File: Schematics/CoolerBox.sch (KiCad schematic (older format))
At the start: 5 parts, among them J5 12VDC Kfz, J6 12VDC Kfz, SW1 S1

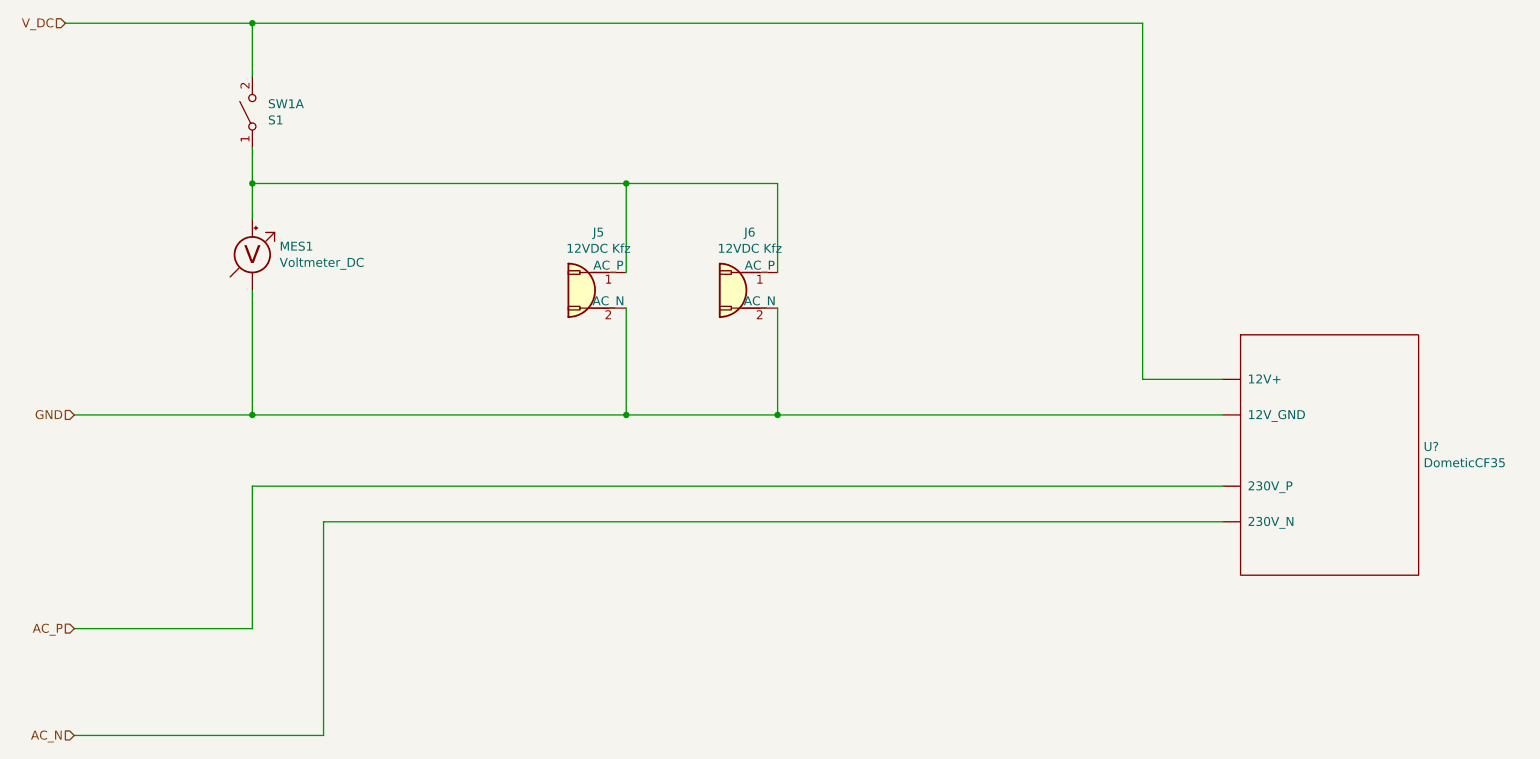
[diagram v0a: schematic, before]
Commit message: add usb charger
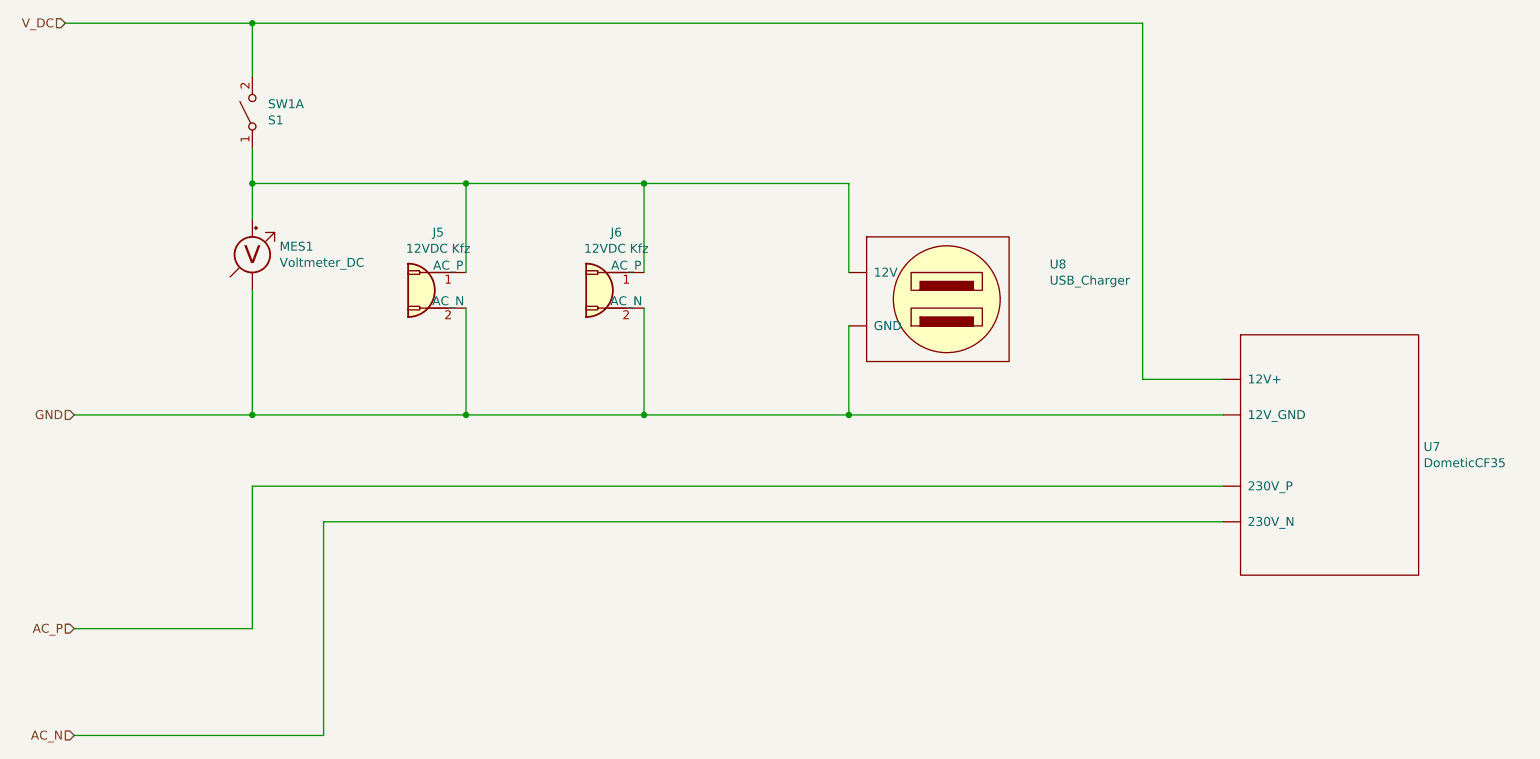
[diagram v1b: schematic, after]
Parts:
- added U8: USB_Charger, symbol MyParts:USB_Charger
- gave numbers to parts that had none: 1
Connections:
- net GND: now also U8.~ (GND)
- net at J5.1 (AC_P), J6.1 (AC_P), MES1.2 (+)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: now also U8.~ (GND)
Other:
- moved on the sheet: J5, J6
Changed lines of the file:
@@
 L Connector:Conn_WallSocket J5
 U 1 1 5EF09B1F
-P 4900 3000
-F 0 "J5" H 4856 3325 50  0000 C CNN
-F 1 "12VDC Kfz" H 4856 3234 50  0000 C CNN
-F 2 "" H 4500 3000 50  0001 C CNN
-F 3 "~" H 4500 3000 50  0001 C CNN
-	1    4900 3000
+P 4000 3000
+F 0 "J5" H 3956 3325 50  0000 C CNN
+F 1 "12VDC Kfz" H 3956 3234 50  0000 C CNN
+F 2 "" H 3600 3000 50  0001 C CNN
+F 3 "~" H 3600 3000 50  0001 C CNN
+	1    4000 3000
 	-1   0    0    -1
 $EndComp
@@
 L Connector:Conn_WallSocket J6
 U 1 1 5EF0A29B
-P 5750 3000
-F 0 "J6" H 5706 3325 50  0000 C CNN
-F 1 "12VDC Kfz" H 5706 3234 50  0000 C CNN
-F 2 "" H 5350 3000 50  0001 C CNN
-F 3 "~" H 5350 3000 50  0001 C CNN
-	1    5750 3000
+P 5000 3000
+F 0 "J6" H 4956 3325 50  0000 C CNN
+F 1 "12VDC Kfz" H 4956 3234 50  0000 C CNN
+F 2 "" H 4600 3000 50  0001 C CNN
+F 3 "~" H 4600 3000 50  0001 C CNN
+	1    5000 3000
 	-1   0    0    -1
 $EndComp
@@
 	3000 3700 3000 3000
 Wire Wire Line
-	3000 2400 5100 2400
+	3000 2400 4200 2400
 Wire Wire Line
-	5100 2400 5100 2900
+	4200 2400 4200 2900
 Connection ~ 3000 2400
 Wire Wire Line
 	3000 2400 3000 2600
 Wire Wire Line
-	5100 2400 5950 2400
+	5200 2400 5200 2900
 Wire Wire Line
-	5950 2400 5950 2900
-Connection ~ 5100 2400
+	3000 3700 4200 3700
 Wire Wire Line
-	3000 3700 5100 3700
-Wire Wire Line
-	5100 3700 5100 3100
+	4200 3700 4200 3100
 Connection ~ 3000 3700
 Wire Wire Line
-	5100 3700 5950 3700
-Wire Wire Line
-	5950 3700 5950 3100
-Connection ~ 5100 3700
+	5200 3700 5200 3100
 Text HLabel 2000 4900 0    50   Input ~ 0
 AC_P
@@
 AC_N
 $Comp
-L MyParts:DometicCF35 U?
+L MyParts:DometicCF35 U7
 U 1 1 5EF0EA96
 P 9000 3350
-F 0 "U?" H 9578 2821 50  0000 L CNN
+F 0 "U7" H 9578 2821 50  0000 L CNN
 F 1 "DometicCF35" H 9578 2730 50  0000 L CNN
 F 2 "" H 9000 3350 50  0001 C CNN
@@
 	3400 4300 8450 4300
 Wire Wire Line
-	3000 1500 8000 1500
-Wire Wire Line
 	8000 1500 8000 3500
 Wire Wire Line
 	8000 3500 8450 3500
 Connection ~ 3000 1500
+$Comp
+L MyParts:USB_Charger U8
+U 1 1 5EF0F9B5
+P 6950 2300
+F 0 "U8" H 7478 1746 50  0000 L CNN
+F 1 "USB_Charger" H 7478 1655 50  0000 L CNN
+F 2 "" H 6950 2300 50  0001 C CNN
+F 3 "" H 6950 2300 50  0001 C CNN
+	1    6950 2300
+	1    0    0    -1
+$EndComp
 Wire Wire Line
-	5950 3700 8450 3700
-Connection ~ 5950 3700
+	6350 2900 6350 2400
+Wire Wire Line
+	6350 3200 6350 3700
+Connection ~ 6350 3700
+Wire Wire Line
+	6350 3700 8450 3700
+Wire Wire Line
+	3000 1500 8000 1500
+Connection ~ 4200 2400
+Connection ~ 4200 3700
+Wire Wire Line
+	4200 2400 5200 2400
+Wire Wire Line
+	4200 3700 5200 3700
+Connection ~ 5200 2400
+Connection ~ 5200 3700
+Wire Wire Line
+	5200 3700 6350 3700
+Wire Wire Line
+	5200 2400 6350 2400
 $EndSCHEMATC

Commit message: add filed
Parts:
- removed U7: DometicCF35, symbol MyParts:DometicCF35
- removed U8: USB_Charger, symbol MyParts:USB_Charger
- renumbered J5 to J?, J6 to J?, MES1 to MES?, SW1 to SW?
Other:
- moved on the sheet: J?
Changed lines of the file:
@@
 $Descr A4 11693 8268
 encoding utf-8
-Sheet 2 3
+Sheet 3 3
 Title ""
 Date ""
@@
 $EndDescr
 $Comp
-L Connector:Conn_WallSocket J5
+L Connector:Conn_WallSocket J?
 U 1 1 5EF09B1F
-P 4000 3000
-F 0 "J5" H 3956 3325 50  0000 C CNN
-F 1 "12VDC Kfz" H 3956 3234 50  0000 C CNN
-F 2 "" H 3600 3000 50  0001 C CNN
-F 3 "~" H 3600 3000 50  0001 C CNN
-	1    4000 3000
+P 4900 3000
+F 0 "J?" H 4856 3325 50  0000 C CNN
+F 1 "12VDC Kfz" H 4856 3234 50  0000 C CNN
+F 2 "" H 4500 3000 50  0001 C CNN
+F 3 "~" H 4500 3000 50  0001 C CNN
+	1    4900 3000
 	-1   0    0    -1
 $EndComp
 $Comp
-L Connector:Conn_WallSocket J6
+L Connector:Conn_WallSocket J?
 U 1 1 5EF0A29B
-P 5000 3000
-F 0 "J6" H 4956 3325 50  0000 C CNN
-F 1 "12VDC Kfz" H 4956 3234 50  0000 C CNN
-F 2 "" H 4600 3000 50  0001 C CNN
-F 3 "~" H 4600 3000 50  0001 C CNN
-	1    5000 3000
+P 5750 3000
+F 0 "J?" H 5706 3325 50  0000 C CNN
+F 1 "12VDC Kfz" H 5706 3234 50  0000 C CNN
+F 2 "" H 5350 3000 50  0001 C CNN
+F 3 "~" H 5350 3000 50  0001 C CNN
+	1    5750 3000
 	-1   0    0    -1
 $EndComp
 $Comp
-L Device:Voltmeter_DC MES1
+L Device:Voltmeter_DC MES?
 U 1 1 5EF0A912
 P 3000 2800
-F 0 "MES1" H 3153 2846 50  0000 L CNN
+F 0 "MES?" H 3153 2846 50  0000 L CNN
 F 1 "Voltmeter_DC" H 3153 2755 50  0000 L CNN
 F 2 "" V 3000 2900 50  0001 C CNN
@@
 $EndComp
 $Comp
-L Switch:SW_DPST_x2 SW1
+L Switch:SW_DPST_x2 SW?
 U 1 1 5EF0B26F
 P 3000 2000
-F 0 "SW1" V 3046 1912 50  0000 R CNN
+F 0 "SW?" V 3046 1912 50  0000 R CNN
 F 1 "S1" V 2955 1912 50  0000 R CNN
 F 2 "" H 3000 2000 50  0001 C CNN
@@
 	3000 3700 3000 3000
 Wire Wire Line
-	3000 2400 4200 2400
+	3000 2400 5100 2400
 Wire Wire Line
-	4200 2400 4200 2900
+	5100 2400 5100 2900
 Connection ~ 3000 2400
 Wire Wire Line
 	3000 2400 3000 2600
 Wire Wire Line
-	5200 2400 5200 2900
+	5100 2400 5950 2400
 Wire Wire Line
-	3000 3700 4200 3700
+	5950 2400 5950 2900
+Connection ~ 5100 2400
 Wire Wire Line
-	4200 3700 4200 3100
+	3000 3700 5100 3700
+Wire Wire Line
+	5100 3700 5100 3100
 Connection ~ 3000 3700
 Wire Wire Line
-	5200 3700 5200 3100
-Text HLabel 2000 4900 0    50   Input ~ 0
-AC_P
-Text HLabel 2000 5500 0    50   Input ~ 0
-AC_N
-$Comp
-L MyParts:DometicCF35 U7
-U 1 1 5EF0EA96
-P 9000 3350
-F 0 "U7" H 9578 2821 50  0000 L CNN
-F 1 "DometicCF35" H 9578 2730 50  0000 L CNN
-F 2 "" H 9000 3350 50  0001 C CNN
-F 3 "" H 9000 3350 50  0001 C CNN
-	1    9000 3350
-	1    0    0    -1
-$EndComp
+	5100 3700 5950 3700
 Wire Wire Line
-	8450 4100 3000 4100
-Wire Wire Line
-	3000 4100 3000 4900
-Wire Wire Line
-	3000 4900 2000 4900
-Wire Wire Line
-	2000 5500 3400 5500
-Wire Wire Line
-	3400 5500 3400 4300
-Wire Wire Line
-	3400 4300 8450 4300
-Wire Wire Line
-	8000 1500 8000 3500
-Wire Wire Line
-	8000 3500 8450 3500
-Connection ~ 3000 1500
-$Comp
-L MyParts:USB_Charger U8
-U 1 1 5EF0F9B5
-P 6950 2300
-F 0 "U8" H 7478 1746 50  0000 L CNN
-F 1 "USB_Charger" H 7478 1655 50  0000 L CNN
-F 2 "" H 6950 2300 50  0001 C CNN
-F 3 "" H 6950 2300 50  0001 C CNN
-	1    6950 2300
-	1    0    0    -1
-$EndComp
-Wire Wire Line
-	6350 2900 6350 2400
-Wire Wire Line
-	6350 3200 6350 3700
-Connection ~ 6350 3700
-Wire Wire Line
-	6350 3700 8450 3700
-Wire Wire Line
-	3000 1500 8000 1500
-Connection ~ 4200 2400
-Connection ~ 4200 3700
-Wire Wire Line
-	4200 2400 5200 2400
-Wire Wire Line
-	4200 3700 5200 3700
-Connection ~ 5200 2400
-Connection ~ 5200 3700
-Wire Wire Line
-	5200 3700 6350 3700
-Wire Wire Line
-	5200 2400 6350 2400
+	5950 3700 5950 3100
+Connection ~ 5100 3700
 $EndSCHEMATC

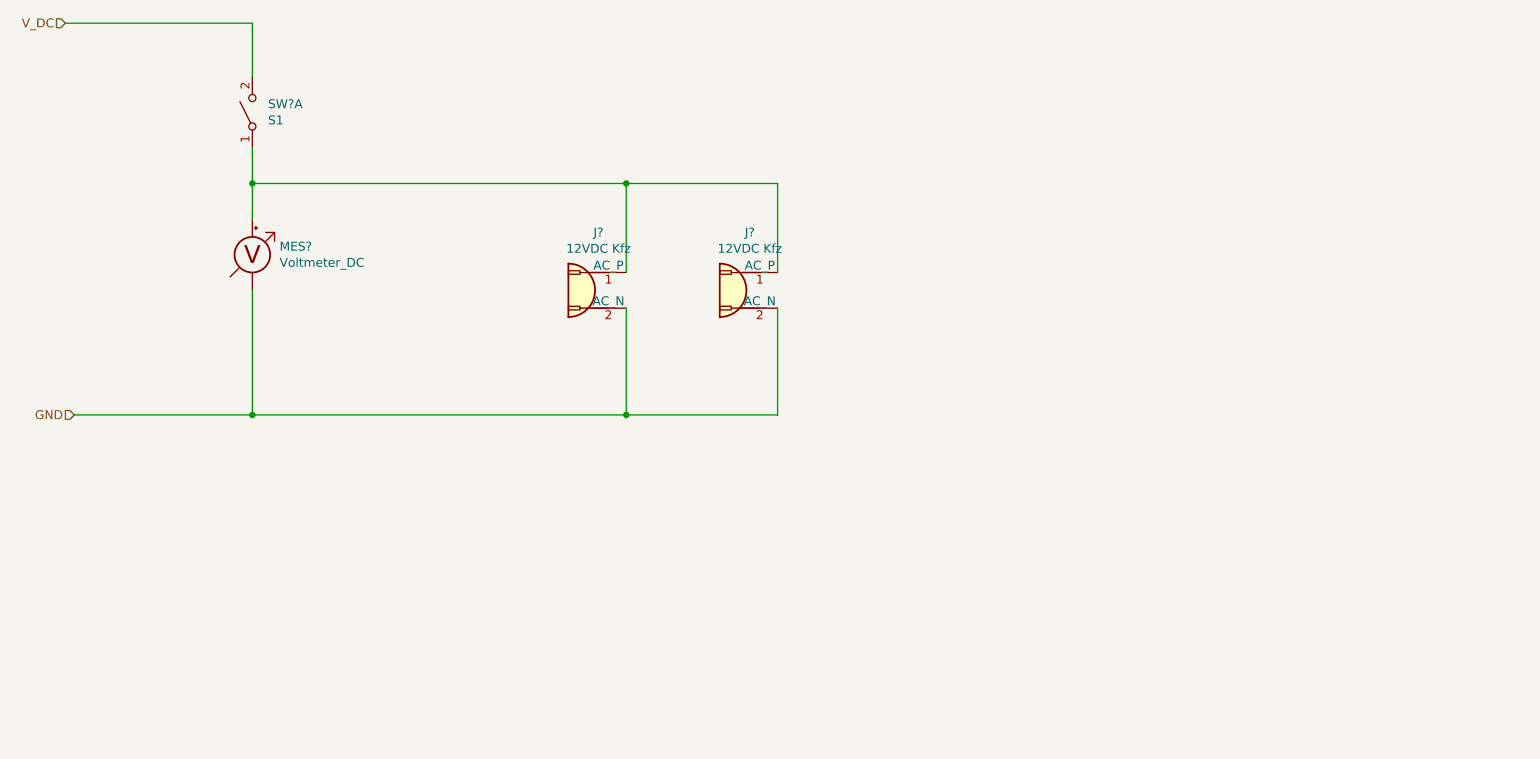
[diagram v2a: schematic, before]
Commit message: add 230V
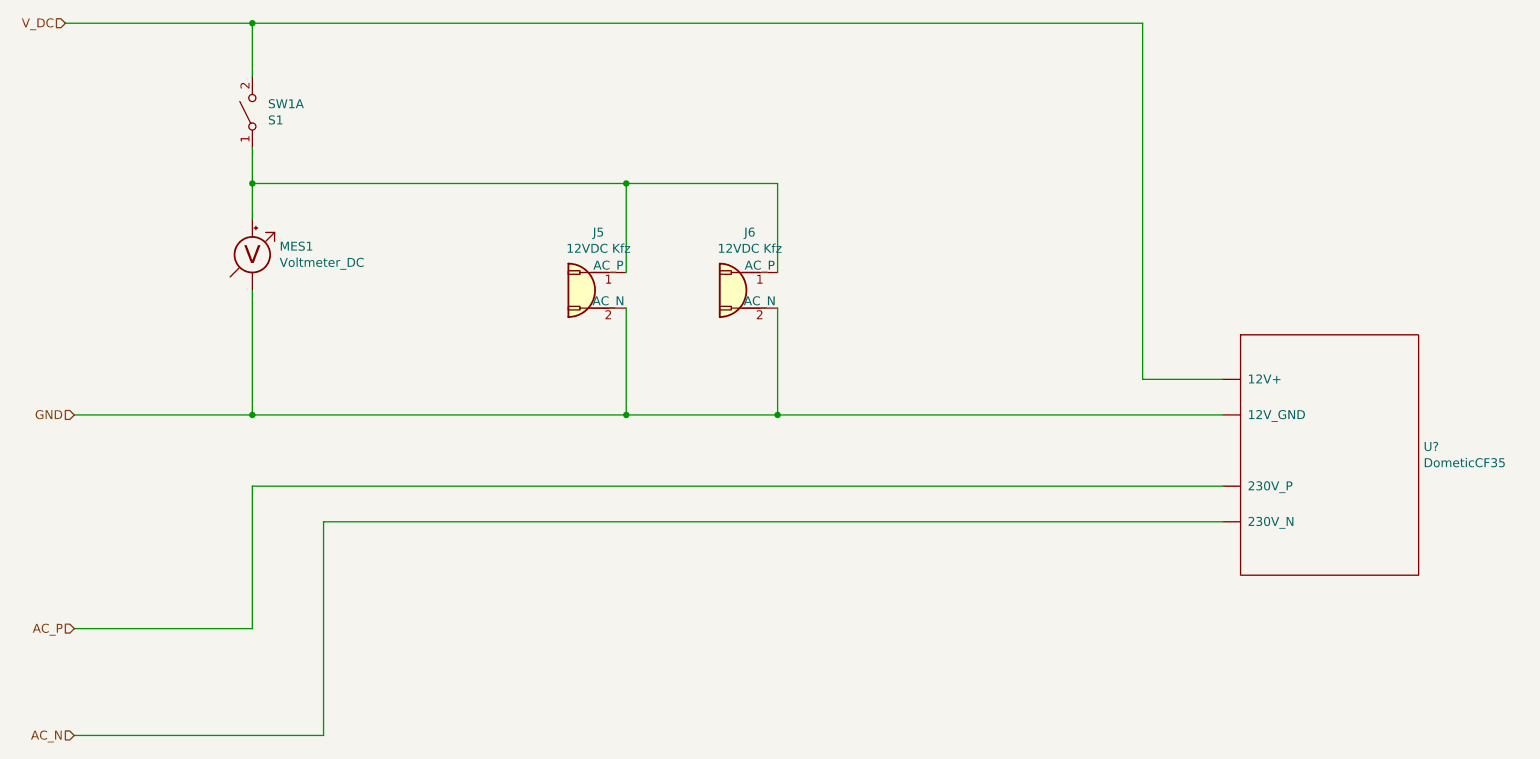
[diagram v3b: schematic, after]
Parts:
- added U?: DometicCF35, symbol MyParts:DometicCF35
- gave numbers to parts that had none: 4
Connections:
- net GND: now also U?.~ (230V_P)
- net V_DC: now also U?.~ (230V_P)
- new net AC_N: U?.~ (230V_P)
- new net AC_P: U?.~ (230V_P)
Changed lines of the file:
@@
 $Descr A4 11693 8268
 encoding utf-8
-Sheet 3 3
+Sheet 2 3
 Title ""
 Date ""
@@
 $EndDescr
 $Comp
-L Connector:Conn_WallSocket J?
+L Connector:Conn_WallSocket J5
 U 1 1 5EF09B1F
 P 4900 3000
-F 0 "J?" H 4856 3325 50  0000 C CNN
+F 0 "J5" H 4856 3325 50  0000 C CNN
 F 1 "12VDC Kfz" H 4856 3234 50  0000 C CNN
 F 2 "" H 4500 3000 50  0001 C CNN
@@
 $EndComp
 $Comp
-L Connector:Conn_WallSocket J?
+L Connector:Conn_WallSocket J6
 U 1 1 5EF0A29B
 P 5750 3000
-F 0 "J?" H 5706 3325 50  0000 C CNN
+F 0 "J6" H 5706 3325 50  0000 C CNN
 F 1 "12VDC Kfz" H 5706 3234 50  0000 C CNN
 F 2 "" H 5350 3000 50  0001 C CNN
@@
 $EndComp
 $Comp
-L Device:Voltmeter_DC MES?
+L Device:Voltmeter_DC MES1
 U 1 1 5EF0A912
 P 3000 2800
-F 0 "MES?" H 3153 2846 50  0000 L CNN
+F 0 "MES1" H 3153 2846 50  0000 L CNN
 F 1 "Voltmeter_DC" H 3153 2755 50  0000 L CNN
 F 2 "" V 3000 2900 50  0001 C CNN
@@
 $EndComp
 $Comp
-L Switch:SW_DPST_x2 SW?
+L Switch:SW_DPST_x2 SW1
 U 1 1 5EF0B26F
 P 3000 2000
-F 0 "SW?" V 3046 1912 50  0000 R CNN
+F 0 "SW1" V 3046 1912 50  0000 R CNN
 F 1 "S1" V 2955 1912 50  0000 R CNN
 F 2 "" H 3000 2000 50  0001 C CNN
@@
 	5950 3700 5950 3100
 Connection ~ 5100 3700
+Text HLabel 2000 4900 0    50   Input ~ 0
+AC_P
+Text HLabel 2000 5500 0    50   Input ~ 0
+AC_N
+$Comp
+L MyParts:DometicCF35 U?
+U 1 1 5EF0EA96
+P 9000 3350
+F 0 "U?" H 9578 2821 50  0000 L CNN
+F 1 "DometicCF35" H 9578 2730 50  0000 L CNN
+F 2 "" H 9000 3350 50  0001 C CNN
+F 3 "" H 9000 3350 50  0001 C CNN
+	1    9000 3350
+	1    0    0    -1
+$EndComp
+Wire Wire Line
+	8450 4100 3000 4100
+Wire Wire Line
+	3000 4100 3000 4900
+Wire Wire Line
+	3000 4900 2000 4900
+Wire Wire Line
+	2000 5500 3400 5500
+Wire Wire Line
+	3400 5500 3400 4300
+Wire Wire Line
+	3400 4300 8450 4300
+Wire Wire Line
+	3000 1500 8000 1500
+Wire Wire Line
+	8000 1500 8000 3500
+Wire Wire Line
+	8000 3500 8450 3500
+Connection ~ 3000 1500
+Wire Wire Line
+	5950 3700 8450 3700
+Connection ~ 5950 3700
 $EndSCHEMATC
